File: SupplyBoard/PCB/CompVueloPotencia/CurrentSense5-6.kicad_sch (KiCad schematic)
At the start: 13 parts, among them U8 INA2180A2

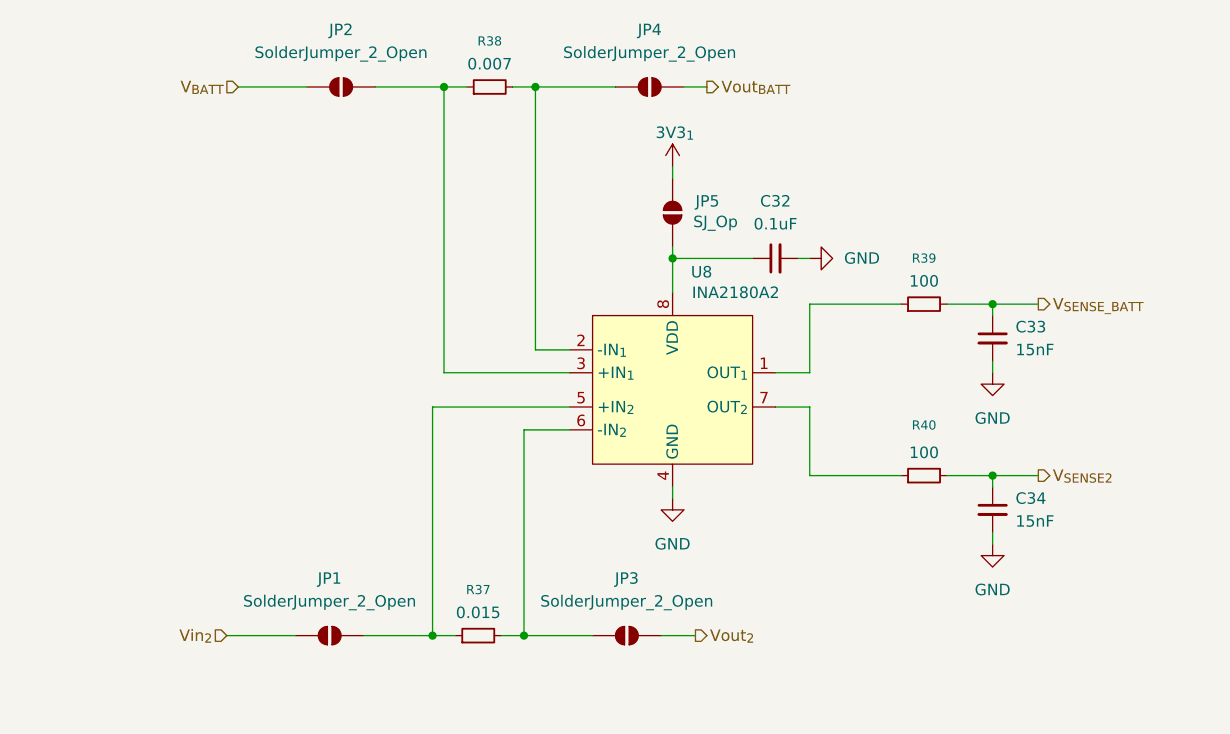
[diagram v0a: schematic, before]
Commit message: SupplyBoard - finish current sense
Finish the Current Sensor Circuit and add more 3.3V out, i change de microcontroles to a mcu that have the exact GPIO's
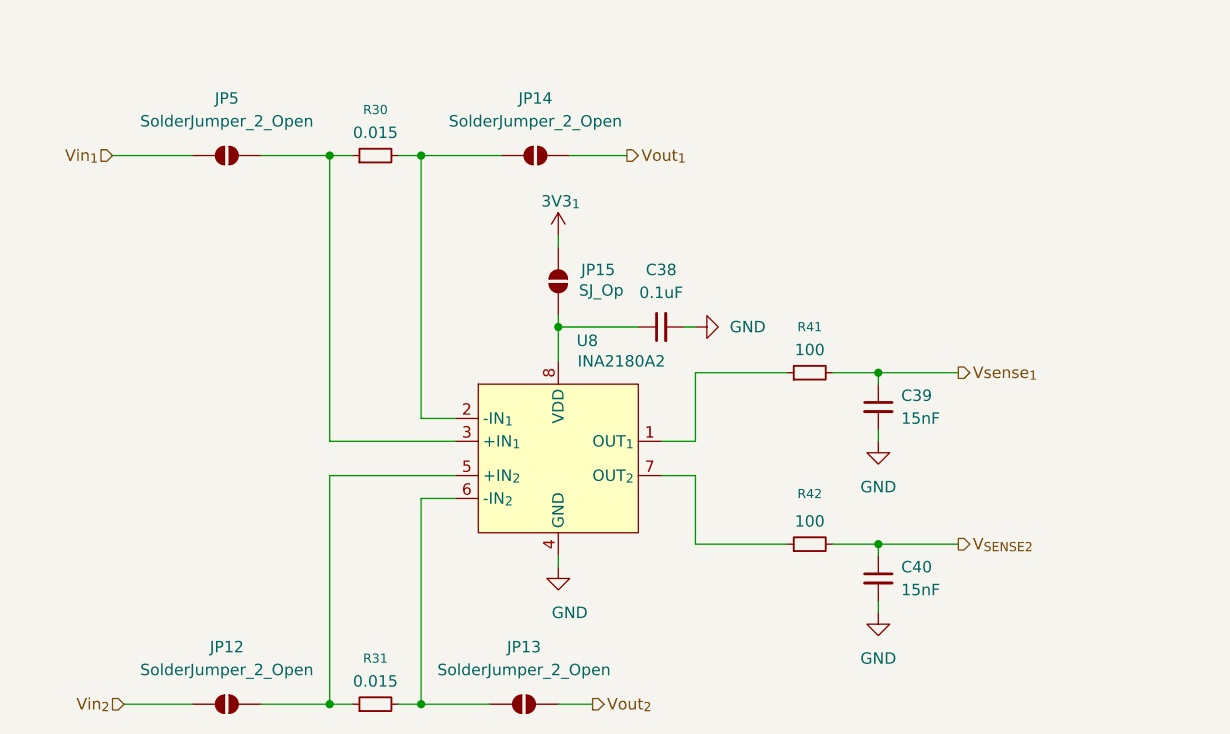
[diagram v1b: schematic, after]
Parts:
- removed C32: 0.1uF, symbol Device:C_Small
- removed C33, C34: 15nF, symbol Device:C_Small
- removed JP1, JP2, JP3, JP4: SolderJumper_2_Open, Jumper:SolderJumper-2_P1.3mm_Open_RoundedPad1.0x1.5mm, symbol Jumper:SolderJumper_2_Open
- removed R37: 0.015, Resistor_SMD:R_1206_3216Metric_Pad1.30x1.75mm_HandSolder, symbol Device:R_Small
- removed R38: 0.007, Resistor_SMD:R_1206_3216Metric_Pad1.30x1.75mm_HandSolder, symbol Device:R_Small
- removed R39, R40: 100, symbol Device:R_Small
- added C38: 0.1uF, symbol Device:C_Small
- added C39, C40: 15nF, symbol Device:C_Small
- added JP12, JP13, JP14: SolderJumper_2_Open, Jumper:SolderJumper-2_P1.3mm_Open_RoundedPad1.0x1.5mm, symbol Jumper:SolderJumper_2_Open
- added JP15: SJ_Op, Jumper:SolderJumper-2_P1.3mm_Open_RoundedPad1.0x1.5mm, symbol Jumper:SolderJumper_2_Open
- added R30, R31: 0.015, Resistor_SMD:R_1206_3216Metric_Pad1.30x1.75mm_HandSolder, symbol Device:R_Small
- added R41, R42: 100, symbol Device:R_Small
- JP5: value SJ_Op -> SolderJumper_2_Open
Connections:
- net 3V3_{1}: now also JP15.2 (B); no longer JP5.2 (B)
- net GND: now also C38.2, C39.2, C40.2
- net V_{SENSE2}: now also C40.1, R42.2
- net Vin_{2}: now also JP12.1 (A)
- net Vout_{2}: now also JP13.2 (B)
- net at U8.3 (+IN_{1}): now also JP5.2 (B), R30.1
- net at U8.2 (-IN_{1}): now also JP14.1 (A), R30.2
- net at U8.5 (+IN_{2}): now also JP12.2 (B), R31.1
- net at U8.7 (OUT_{2}): now also R42.1
- net at U8.6 (-IN_{2}): now also JP13.1 (A), R31.2
- net at U8.1 (OUT_{1}): now also R41.1
- net at U8.8 (VDD): now also C38.1, JP15.1 (A); no longer JP5.1 (A)
- new net Vin_{1}: JP5.1 (A)
- new net Vout_{1}: JP14.2 (B)
- new net Vsense_{1}: C39.1, R41.2
